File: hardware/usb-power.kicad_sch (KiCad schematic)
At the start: 6 parts, among them IC1 NCV1117ST33T3G, J1 USB_C_Receptacle_USB2.0_16P

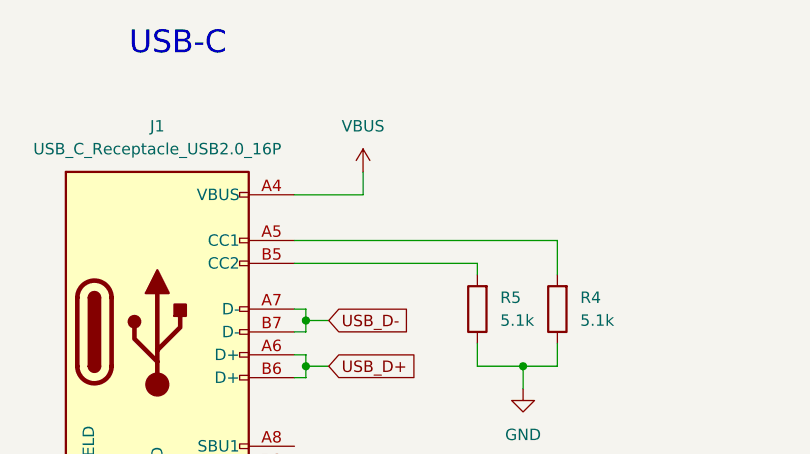
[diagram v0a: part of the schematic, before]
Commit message: Completed ADC, new components and test points
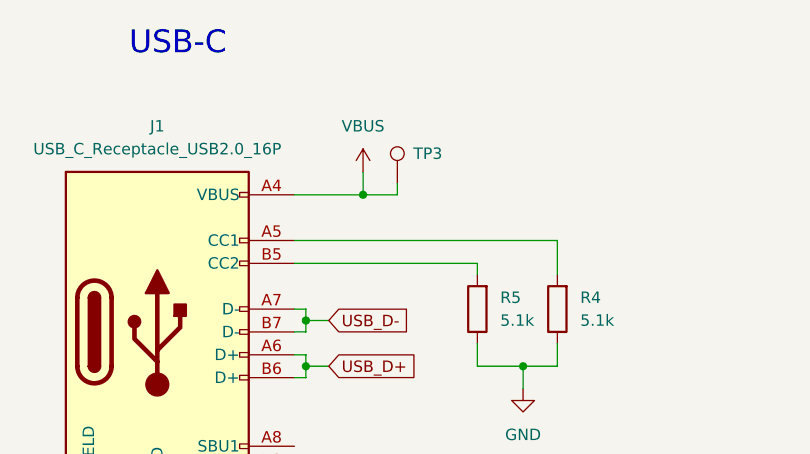
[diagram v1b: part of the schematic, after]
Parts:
- added TP3: TestPoint, TestPoint:TestPoint_Pad_D1.0mm, symbol Connector:TestPoint
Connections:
- net VBUS: now also TP3.1
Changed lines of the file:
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@@
+	)
+	(junction
+		(at 72.39 44.45)
+		(diameter 0)
+		(color 0 0 0 0)
 	)
 	(junction
@@
 	(wire
 		(pts
+			(xy 76.2 43.18) (xy 76.2 44.45)
+		)
+		(stroke
+			(width 0)
+			(type default)
+		)
+	)
+	(wire
+		(pts
 			(xy 72.39 44.45) (xy 72.39 41.91)
+		)
+		(stroke
+			(width 0)
+			(type default)
+		)
+	)
+	(wire
+		(pts
+			(xy 76.2 44.45) (xy 72.39 44.45)
 		)
 		(stroke
@@
 					(unit 1)
 				)
+			)
+		)
+	)
+	(symbol
+		(lib_id "Connector:TestPoint")
+		(at 76.2 43.18 0)
+		(unit 1)
+		(body_style 1)
+		(exclude_from_sim no)
+		(in_bom yes)
+		(on_board yes)
+		(in_pos_files yes)
+		(dnp no)
+		(property "Reference" "TP3"
+			(at 77.978 39.878 0)
+			(show_name no)
+			(do_not_autoplace no)
+			(effects
+				(font
+					(size 1.27 1.27)
+				)
+				(justify left)
+			)
+		)
+		(property "Value" "TestPoint"
+			(at 78.74 41.1479 0)
+			(hide yes)
+			(show_name no)
+			(do_not_autoplace no)
+			(effects
+				(font
+					(size 1.27 1.27)
+				)
+				(justify left)
+			)
+		)
+		(property "Footprint" "TestPoint:TestPoint_Pad_D1.0mm"
+			(at 81.28 43.18 0)
+			(hide yes)
+			(show_name no)
+			(do_not_autoplace no)
+			(effects
+				(font
+					(size 1.27 1.27)
+				)
+			)
+		)
+		(property "Datasheet" ""
+			(at 81.28 43.18 0)
+			(hide yes)
+			(show_name no)
+			(do_not_autoplace no)
+			(effects
+				(font
+					(size 1.27 1.27)
+				)
+			)
+		)
+		(property "Description" "test point"
+			(at 76.2 43.18 0)
+			(hide yes)
+			(show_name no)
+			(do_not_autoplace no)
+			(effects
+				(font
+					(size 1.27 1.27)
+				)
+			)
+		)
+		(pin "1"
+		)
+		(instances
+			(project "Stuttgart"
+				(path "/6d354744-ce95-4d5c-b7ae-1990dae66f7b/304bef4f-add0-487c-b718-54fa10a4bc8f"
+					(reference "TP3")
+					(unit 1)
+				)
